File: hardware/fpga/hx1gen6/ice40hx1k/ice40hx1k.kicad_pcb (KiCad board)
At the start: 2 copper layers, 59 parts, among them J1 Conn_01x06_Male, J2 Conn_01x20_Male, J3 Conn_01x20_Male, U1 AT25SF081-SSHD-X, U2 ICE40HX1K-VQ100(VQFP100), U3 LTC3406ES5, U4 ATSAMD11D14A-M, U5 LTC3406ES5, X1 ASE-10MHz, X2 ASE-10MHz, X3 ASE-10MHz, X4 USBFCI_10103594_MILL

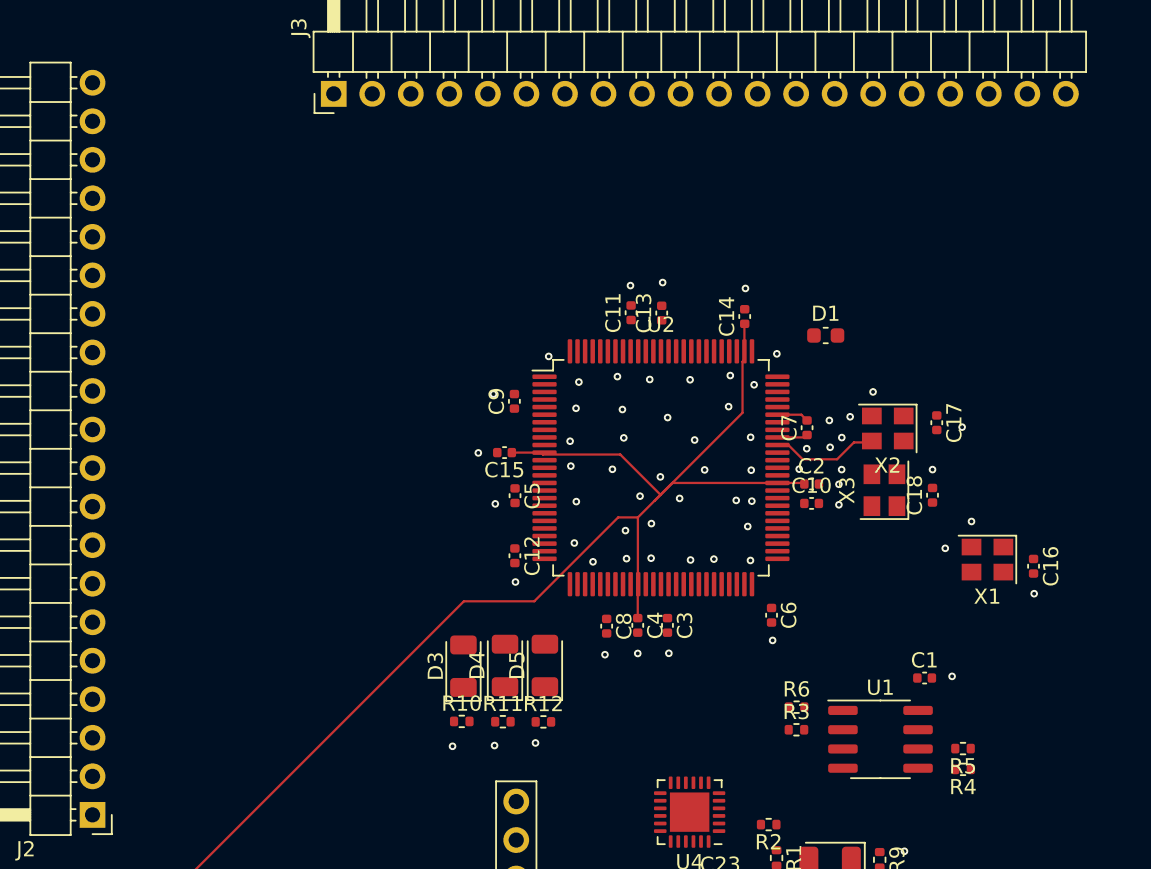
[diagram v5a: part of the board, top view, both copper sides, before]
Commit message: preparing FSK and phase experiments: started HX1K gen6 brd
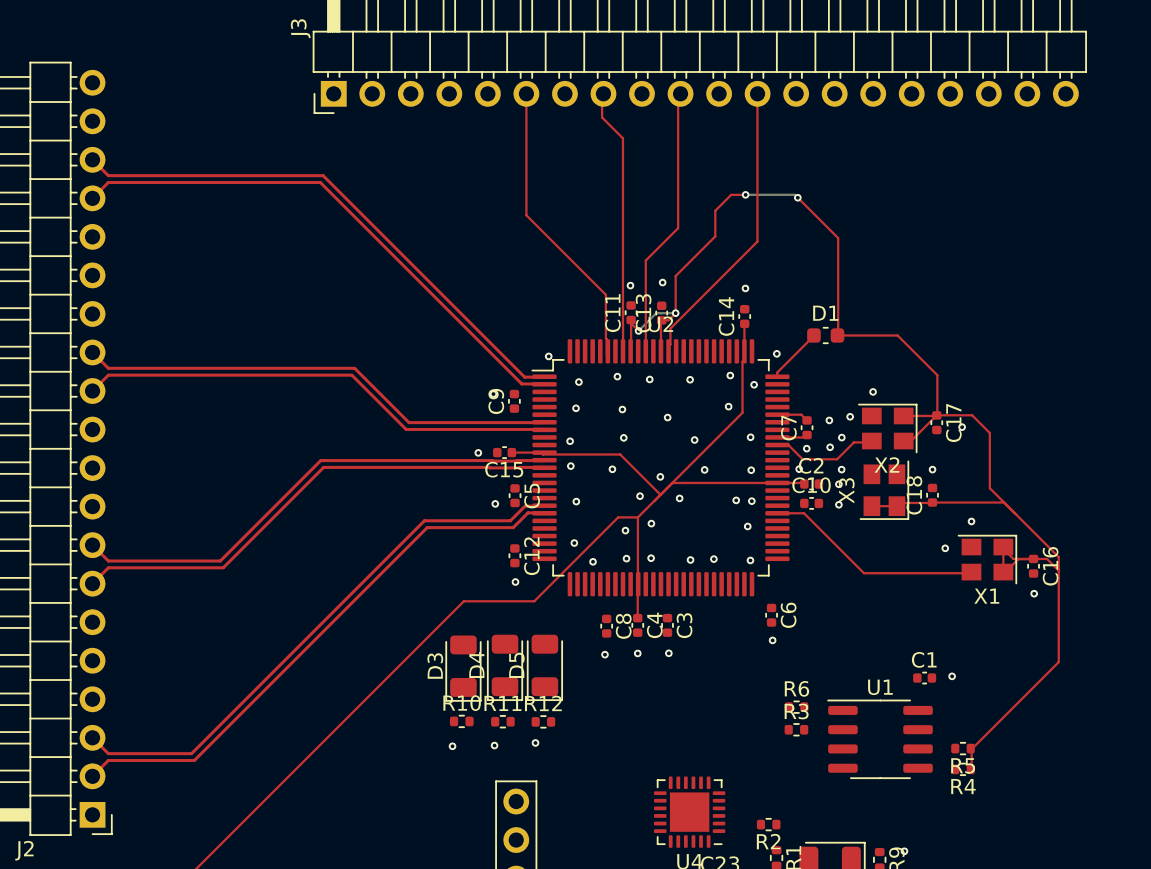
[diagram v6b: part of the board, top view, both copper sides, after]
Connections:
- net IO12_6A renamed IO12_6N
- net IO13_6B renamed IO12_6P
- net IO18_8A renamed IO18_8N
- net IO19_8B renamed IO18_8P
- net IO1_1A renamed IO1_1N
- net IO2_1A renamed IO1_1P
- net IO7_3A renamed IO7_3N
- net IO8_3B renamed IO7_3P
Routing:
- net +3V3: track 1.97 -> 98.7 mm, vias 0 -> 4
- net IO18_8P: track 0.00 -> 37.0 mm
- net IO18_8N: track 0.00 -> 37.0 mm
- net IO1_1N: track 0.00 -> 35.7 mm
- net IO1_1P: track 0.00 -> 35.7 mm
- net IO12_6N: track 0.00 -> 33.0 mm
- net IO12_6P: track 0.00 -> 33.0 mm
- net IO7_3N: track 0.00 -> 31.7 mm
- net IO7_3P: track 0.00 -> 31.7 mm
- net pwm_tx_1: track 0.00 -> 19.5 mm
- net pwm_tx_4: track 0.00 -> 19.3 mm
- net pwm_tx_3: track 0.00 -> 18.0 mm
- net pwm_tx_2: track 0.00 -> 17.6 mm
- net clock_2: track 0.00 -> 14.4 mm
- net Net-(D1-Pad1): track 0.00 -> 3.56 mm

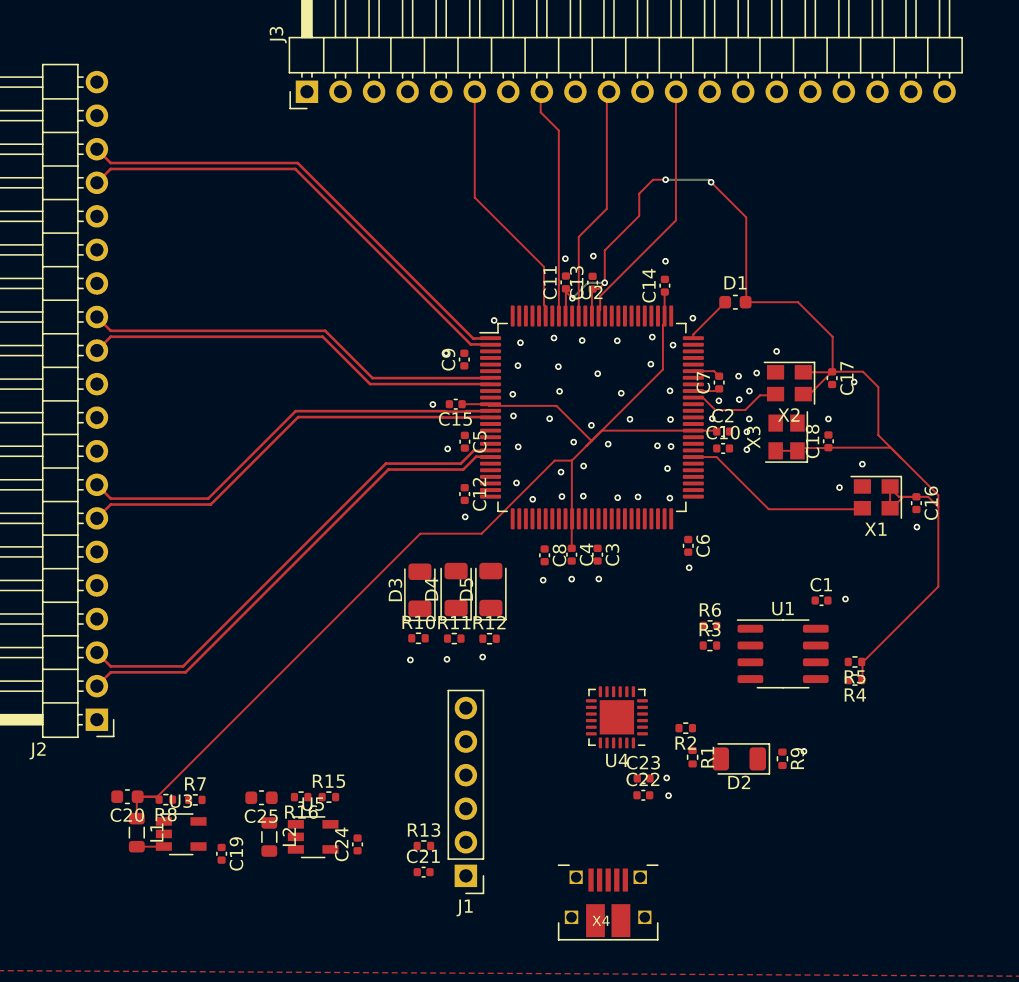
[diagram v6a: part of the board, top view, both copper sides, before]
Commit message: preparing FSK and phase experiments: started HX1K gen6 brd
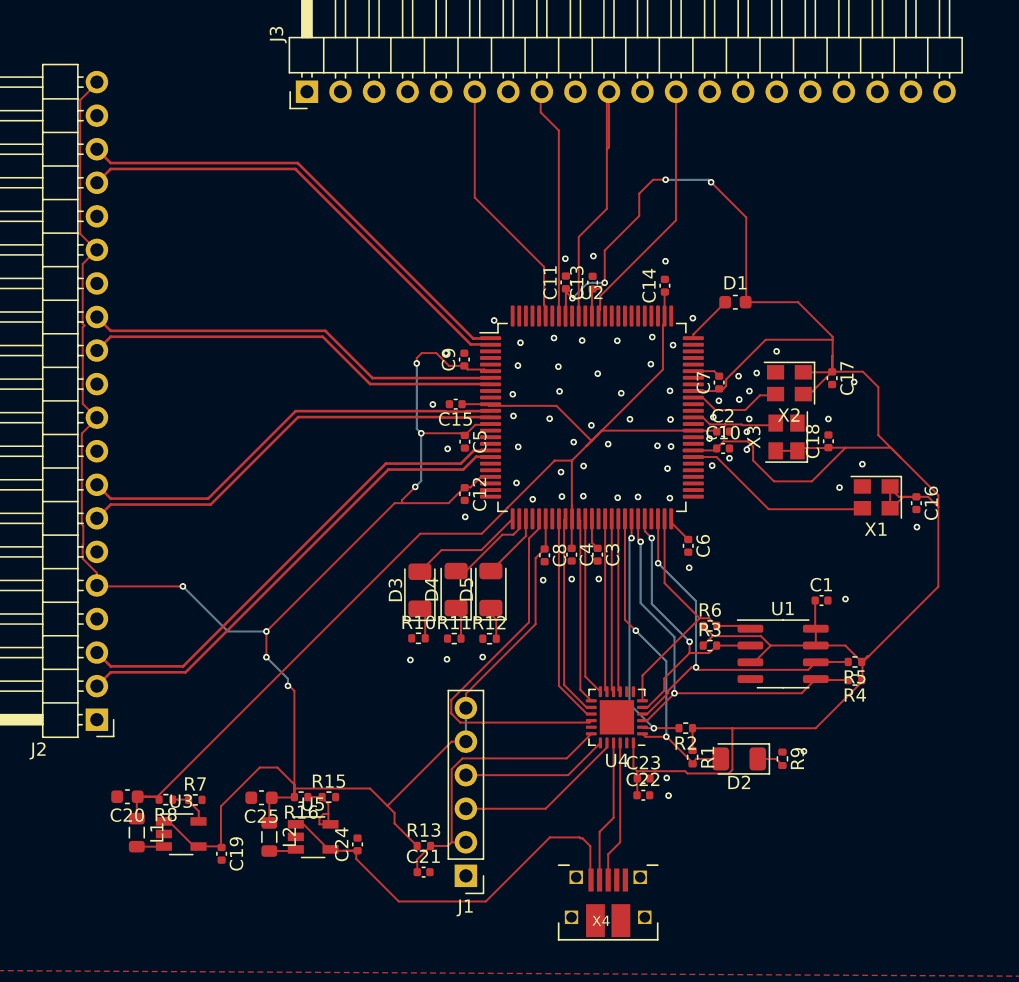
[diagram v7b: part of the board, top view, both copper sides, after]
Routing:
- net +3V3: track 98.7 -> 360.5 mm, vias 4 -> 11
- net fpga_spi_out: track 0.00 -> 31.2 mm, vias 0 -> 2
- net +5V: track 0.00 -> 31.1 mm
- net spi_clk: track 0.00 -> 29.9 mm, vias 0 -> 2
- net sercom1_pad1: track 0.00 -> 28.4 mm
- net cdone: track 0.00 -> 24.8 mm, vias 0 -> 2
- net swd_rst: track 0.00 -> 22.4 mm
- net fpga_spi_in: track 0.00 -> 22.2 mm, vias 0 -> 2
- net spi_cs: track 0.00 -> 20.8 mm
- net creset: track 0.00 -> 19.5 mm, vias 0 -> 2
- net sercom1_pad0: track 0.00 -> 16.0 mm
- net sercom1_pad3: track 0.00 -> 15.4 mm
- net sercom1_pad2: track 0.00 -> 14.2 mm
- net sercom2_pad1: track 0.00 -> 13.6 mm
- net sercom2_pad3: track 0.00 -> 13.1 mm
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
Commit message: preparing FSK and phase experiments: started HX1K gen6 brd: r6try1
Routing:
- net +3V3: track 360.5 -> 414.9 mm, vias 11 -> 14
- net GND: vias 72 -> 472
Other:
- board outline added: 74.3 x 67.6 mm
